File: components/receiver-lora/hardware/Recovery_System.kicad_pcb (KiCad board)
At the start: 2 copper layers, 54.6 x 89.2 mm, 5 parts, among them J1 Conn_Coaxial_Small, U1 ESP32-C3-DevKitM-1, U2 NEO-M8N, U3 RFM95W-868S2

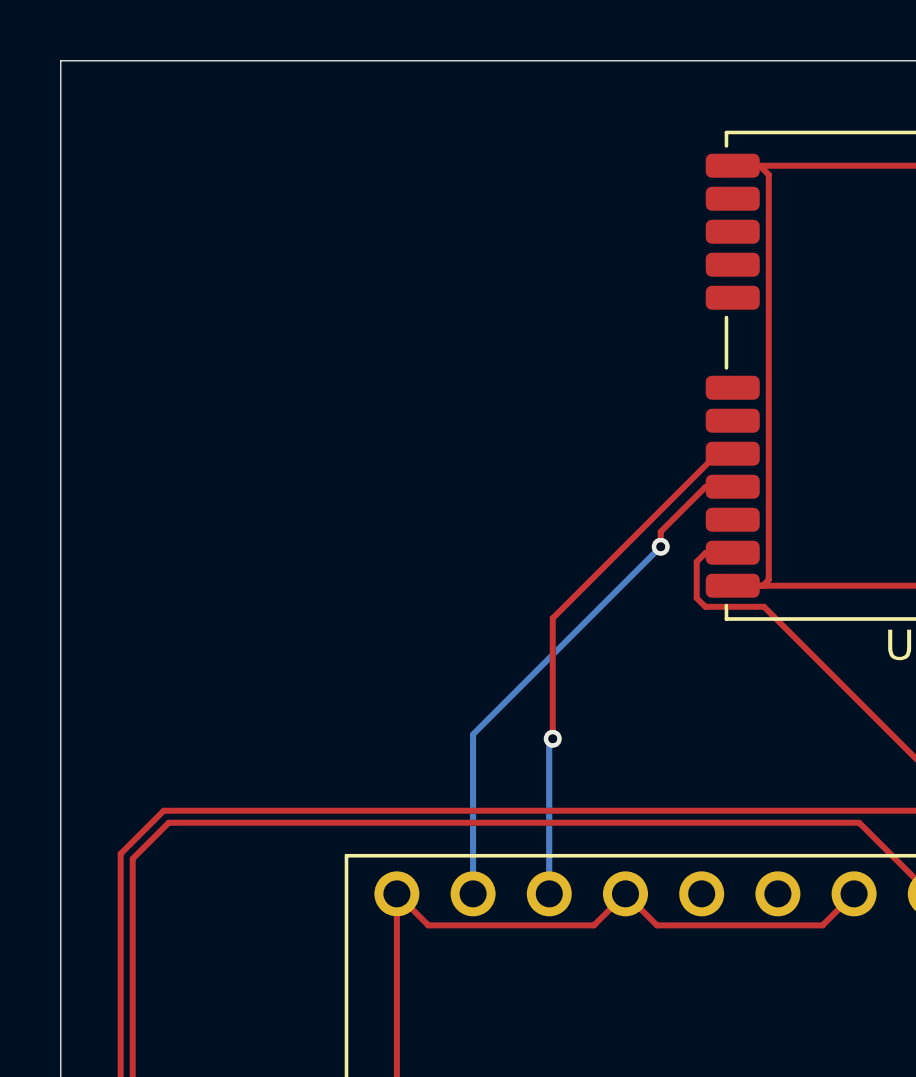
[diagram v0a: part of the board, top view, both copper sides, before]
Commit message: Modify net connections and add resistor and buzzer
Updated net connections and added new components including a resistor and a buzzer with their properties.
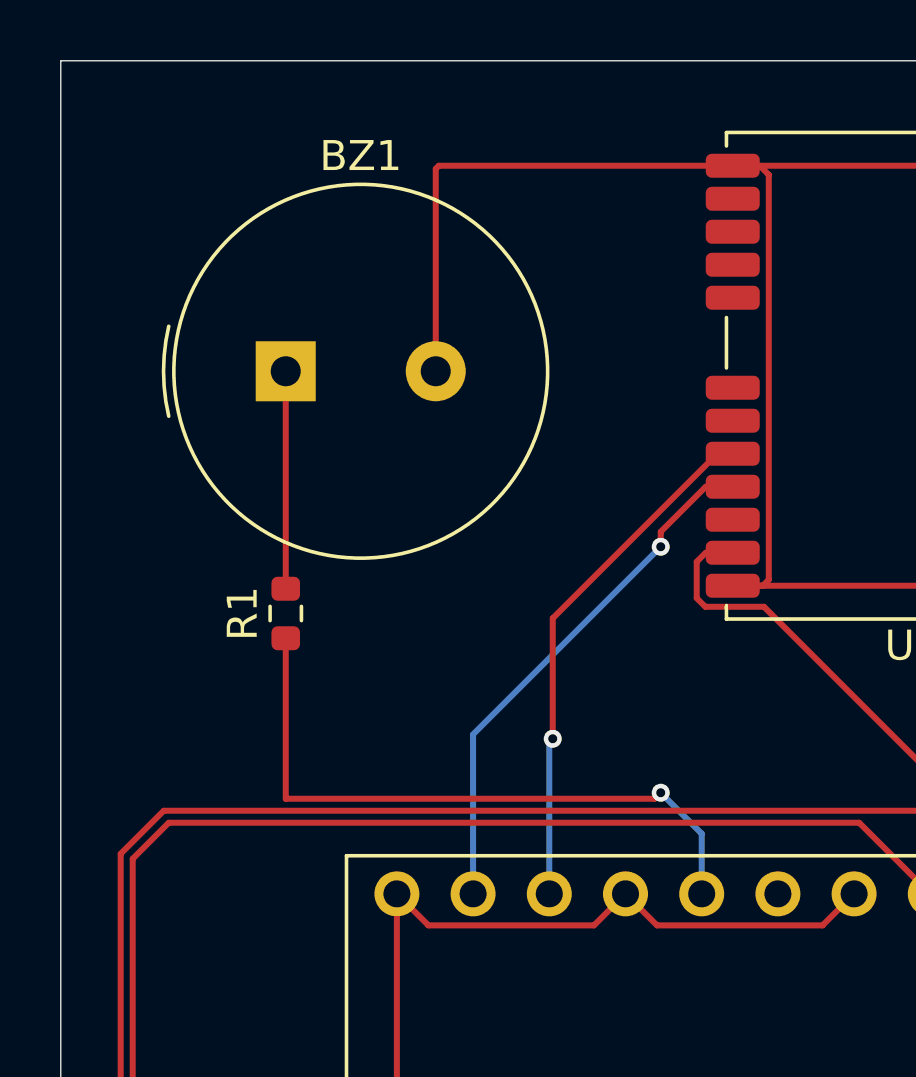
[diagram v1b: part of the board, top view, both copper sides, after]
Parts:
- added BZ1: Buzzer, Buzzer_Beeper:Buzzer_TDK_PS1240P02BT_D12.2mm_H6.5mm, F.Cu at (120.5, 59.8)
- added R1: R, Resistor_SMD:R_0603_1608Metric, F.Cu at (120.5, 67.8)
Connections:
- U1 pad 26: unconnected-(U1-IO9-Pad26) -> Net-(U1-IO9)
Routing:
- net Net-(U1-IO9): track 0.00 -> 21.9 mm, vias 0 -> 1
- net Net-(BT1--): track 323.5 -> 340.2 mm
- net Net-(BZ1-+): track 0.00 -> 7.25 mm

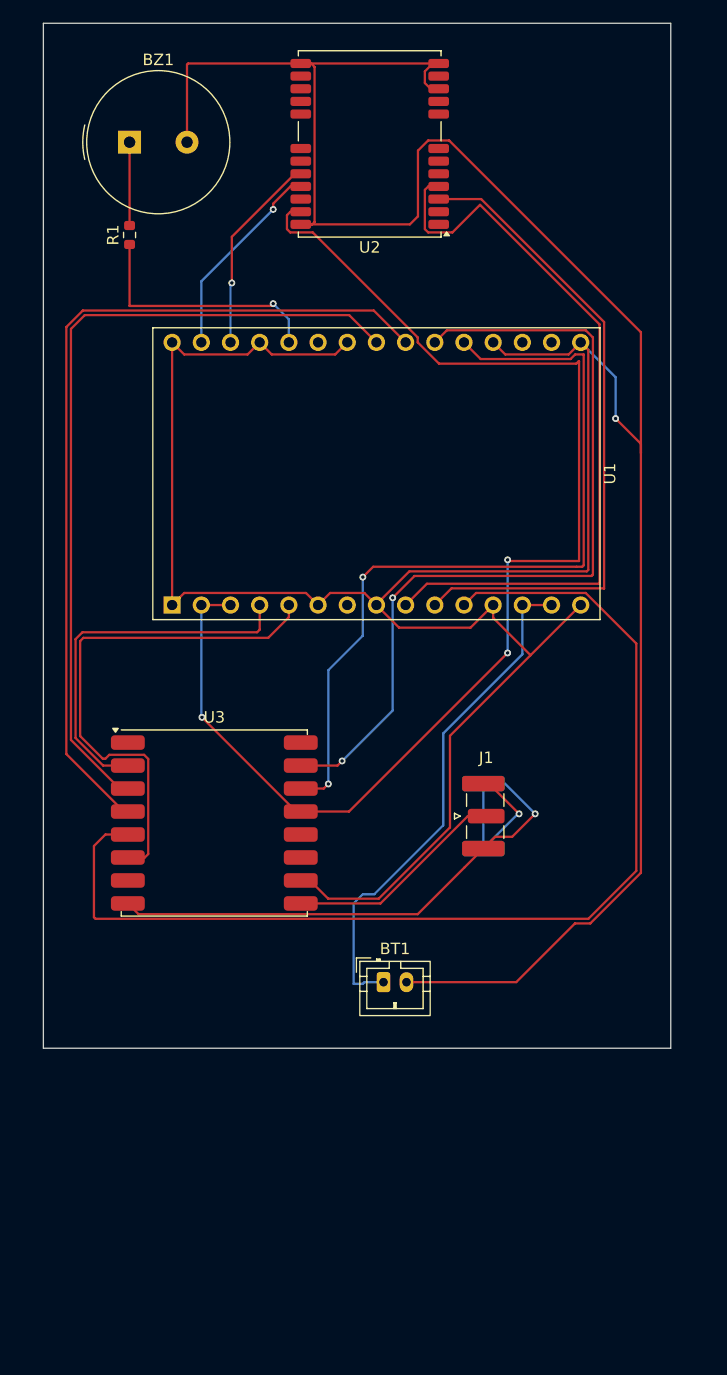
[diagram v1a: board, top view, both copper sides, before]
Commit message: Update Recovery_System.kicad_pcb
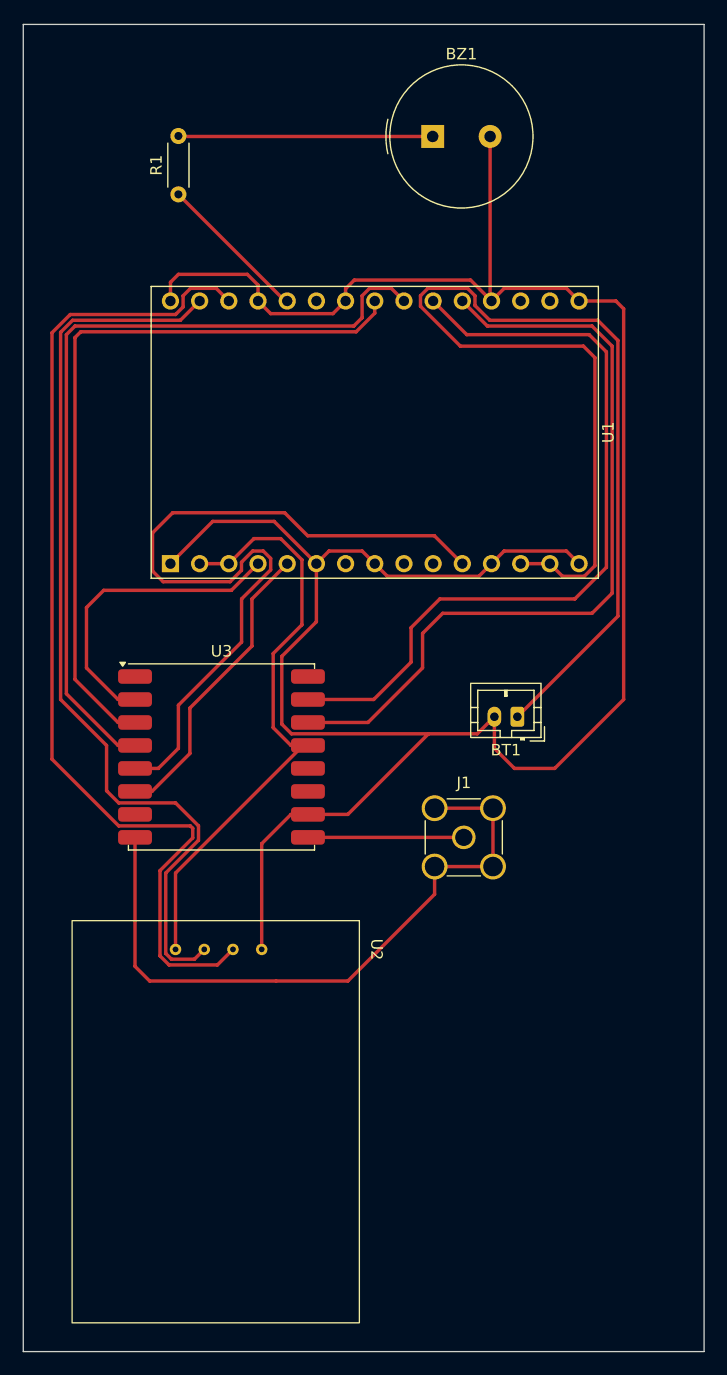
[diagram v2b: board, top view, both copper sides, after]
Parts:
- J1: footprint Connector_Coaxial:SMA_Samtec_SMA-J-P-H-ST-EM1_EdgeMount -> Connector_Coaxial:SMA_Amphenol_901-144_Vertical
- R1: footprint Resistor_SMD:R_0603_1608Metric -> Resistor_THT:R_Axial_DIN0204_L3.6mm_D1.6mm_P5.08mm_Horizontal
- U2: value NEO-M8N -> ~; footprint RF_GPS:ublox_NEO -> Footprint Lybrary:GPS
- moved U2 87.8 mm to (136.0, 147.5), turned to -90 degrees
- moved BZ1 26.4 mm to (146.9, 59.2)
- moved BT1 25.9 mm to (154.2, 109.8), turned to 180 degrees
- moved U3 5.78 mm to (128.5, 113.2)
- moved R1 5.53 mm to (124.8, 64.3)
- moved U1 3.60 mm to (124.1, 96.4)
- moved J1 2.69 mm to (149.6, 120.2)
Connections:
- U1 pad 10: Net-(U1-IO1) -> unconnected-(U1-IO1-Pad10)
- U1 pad 9: Net-(U1-IO0) -> unconnected-(U1-IO0-Pad9)
- U2 pad 1: unconnected-(U2-~{SAFEBOOT}-Pad1) -> Net-(BT1--)
- U2 pad 2: unconnected-(U2-D_SEL-Pad2) -> Net-(U1-RX)
- U2 pad 3: Net-(U1-IO1) -> Net-(U1-TX)
- U2 pad 4: Net-(U1-IO0) -> Net-(U2-VCC)
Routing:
- net Net-(BT1--): track 340.2 -> 216.6 mm, vias 1 -> 0
- net Net-(U1-RX): track 17.5 -> 89.4 mm, vias 1 -> 0
- net Net-(U1-IO0): track 65.6 -> 0.00 mm
- net Net-(U1-TX): track 17.7 -> 80.2 mm, vias 1 -> 0
- net Net-(U2-VCC): track 113.0 -> 52.6 mm, vias 3 -> 0
- net Net-(U1-IO1): track 57.4 -> 0.00 mm
- net Net-(BT1-+): track 44.8 -> 99.5 mm
- net Net-(U1-IO10): track 95.6 -> 69.6 mm
- net Net-(U1-IO3): track 45.6 -> 26.2 mm
- net Net-(BZ1-+): track 7.25 -> 22.1 mm
- net Net-(U1-IO9): track 21.9 -> 13.3 mm, vias 1 -> 0
- net Net-(U1-IO7): track 70.5 -> 64.6 mm
- net Net-(J1-In): track 19.3 -> 13.6 mm
- net Net-(U1-IO2): track 32.7 -> 27.1 mm
- net Net-(U1-IO5): track 73.1 -> 68.2 mm, vias 2 -> 0
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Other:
- board size 54.6 x 89.2 mm -> 59.2 x 115.5 mm
